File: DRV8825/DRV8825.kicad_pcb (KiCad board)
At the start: 2 copper layers, 2 parts, among them U1 DRV8825PWPR

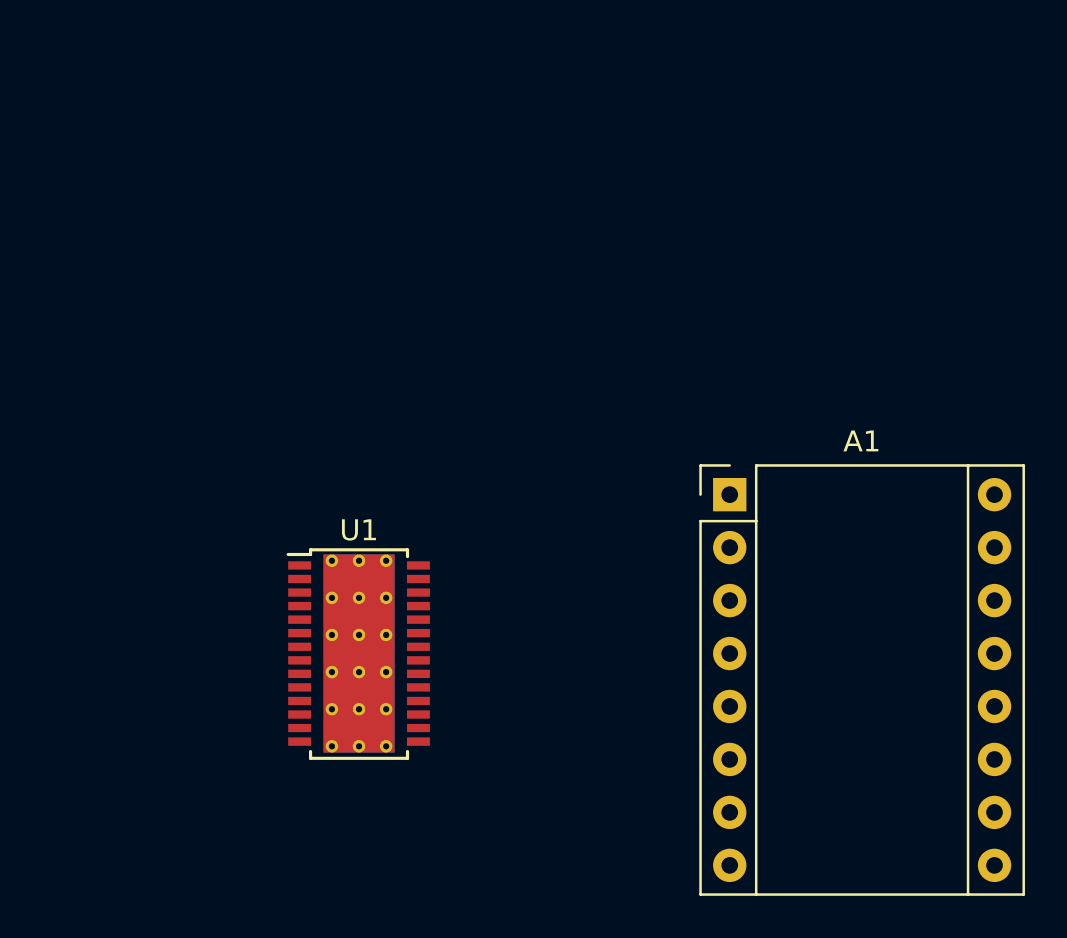
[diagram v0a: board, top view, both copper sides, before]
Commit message: FINISH DRV8825
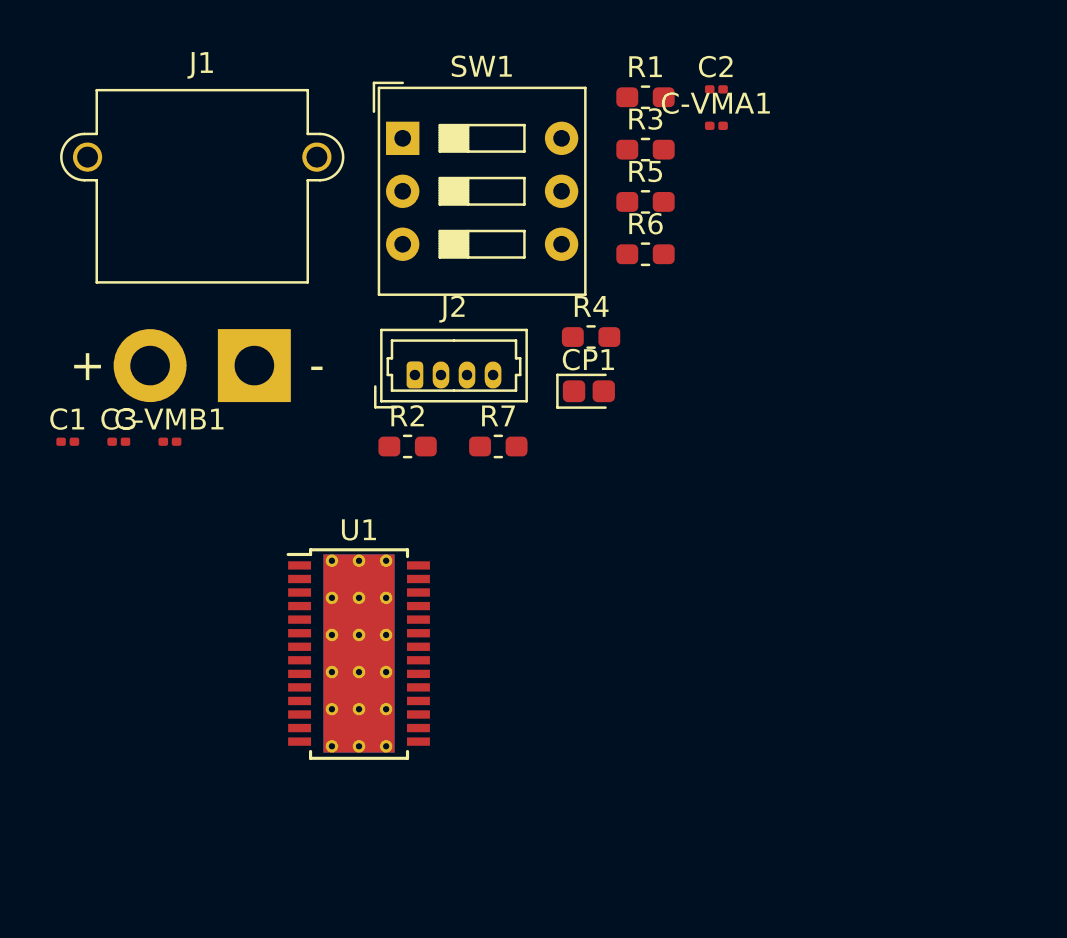
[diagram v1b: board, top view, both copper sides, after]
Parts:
- removed A1: Pololu_Breakout_DRV8825, Module:Pololu_Breakout-16_15.2x20.3mm
- added C-VMA1: 0.1uF, Capacitor_SMD:C_0201_0603Metric, F.Cu at (79.4, 34.4)
- added C-VMB1: 0.1uF, Capacitor_SMD:C_0201_0603Metric, F.Cu at (53.2, 49.5)
- added C1: 0.01uF, Capacitor_SMD:C_0201_0603Metric, F.Cu at (48.3, 49.5)
- added C2: 0.1uF, Capacitor_SMD:C_0201_0603Metric, F.Cu at (79.4, 32.6)
- added C3: 0.47uF, Capacitor_SMD:C_0201_0603Metric, F.Cu at (50.7, 49.5)
- added CP1: 100uF, Capacitor_Tantalum_SMD:CP_EIA-1608-08_AVX-J, F.Cu at (73.3, 47.1)
- added J1: Conn_Coaxial_Power, Connector_AMASS:AMASS_XT30PW-M_1x02_P2.50mm_Horizontal, F.Cu at (57.2, 45.9)
- added J2: Conn_01x04_Male, Connector_Molex:Molex_PicoBlade_53047-0410_1x04_P1.25mm_Vertical, F.Cu at (64.9, 46.3)
- added R1: 1M, Resistor_SMD:R_0603_1608Metric_Pad1.05x0.95mm_HandSolder, F.Cu at (76.0, 33.0)
- added R2: 50K, Resistor_SMD:R_0603_1608Metric_Pad1.05x0.95mm_HandSolder, F.Cu at (64.6, 49.8)
- added R3: 30K, Resistor_SMD:R_0603_1608Metric_Pad1.05x0.95mm_HandSolder, F.Cu at (76.0, 35.5)
- added R4: 200m, Resistor_SMD:R_0603_1608Metric_Pad1.05x0.95mm_HandSolder, F.Cu at (73.4, 44.5)
- added R5: 200m, Resistor_SMD:R_0603_1608Metric_Pad1.05x0.95mm_HandSolder, F.Cu at (76.0, 38.0)
- added R6: 10K, Resistor_SMD:R_0603_1608Metric_Pad1.05x0.95mm_HandSolder, F.Cu at (76.0, 40.5)
- added R7: 10K, Resistor_SMD:R_0603_1608Metric_Pad1.05x0.95mm_HandSolder, F.Cu at (68.9, 49.8)
- added SW1: SW_DIP_x03, Button_Switch_THT:SW_DIP_SPSTx03_Slide_9.78x9.8mm_W7.62mm_P2.54mm, F.Cu at (64.3, 35.0)
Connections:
- net Net-(U1-Pad14) renamed GND
- net Net-(U1-Pad20) renamed /DIR
- net Net-(U1-Pad22) renamed /STEP
- U1 pad 11: Net-(U1-Pad11) -> +12V
- U1 pad 12: Net-(U1-Pad12) -> Net-(R2-Pad2)
- U1 pad 13: Net-(U1-Pad13) -> Net-(R2-Pad2)
- U1 pad 15: Net-(U1-Pad15) -> /V3P3OUT
- U1 pad 16: Net-(U1-Pad16) -> +5V
- U1 pad 17: Net-(U1-Pad17) -> +5V
- U1 pad 24: Net-(U1-Pad24) -> /MS1
- U1 pad 25: Net-(U1-Pad25) -> /MS2
- U1 pad 26: Net-(U1-Pad26) -> /MS2
- U1 pad 4: Net-(U1-Pad4) -> +12V
